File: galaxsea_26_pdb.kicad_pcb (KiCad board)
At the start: 2 copper layers, 80 x 50 mm, 27 parts, among them J1 Conn_01x10_Pin, J2 Conn_01x10_Pin, J3 Conn_01x10_Pin, U1 TPS54531DDA

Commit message: Dimensions
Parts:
- moved G*** 40.8 mm to (116.4, 63.4)
- moved D2 5.60 mm to (131.1, 71.7)
- moved D3 5.60 mm to (136.5, 71.7)
- moved R4 5.60 mm to (131.1, 76.0)
- moved R5 5.60 mm to (136.5, 76.0)
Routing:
- net /BDC Module/BDC_VOUT: track 86.6 -> 80.4 mm
- net /BDC Module/BDC_VIN_Fuse: track 29.7 -> 24.7 mm
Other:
- outline, holes or cut-outs redrawn

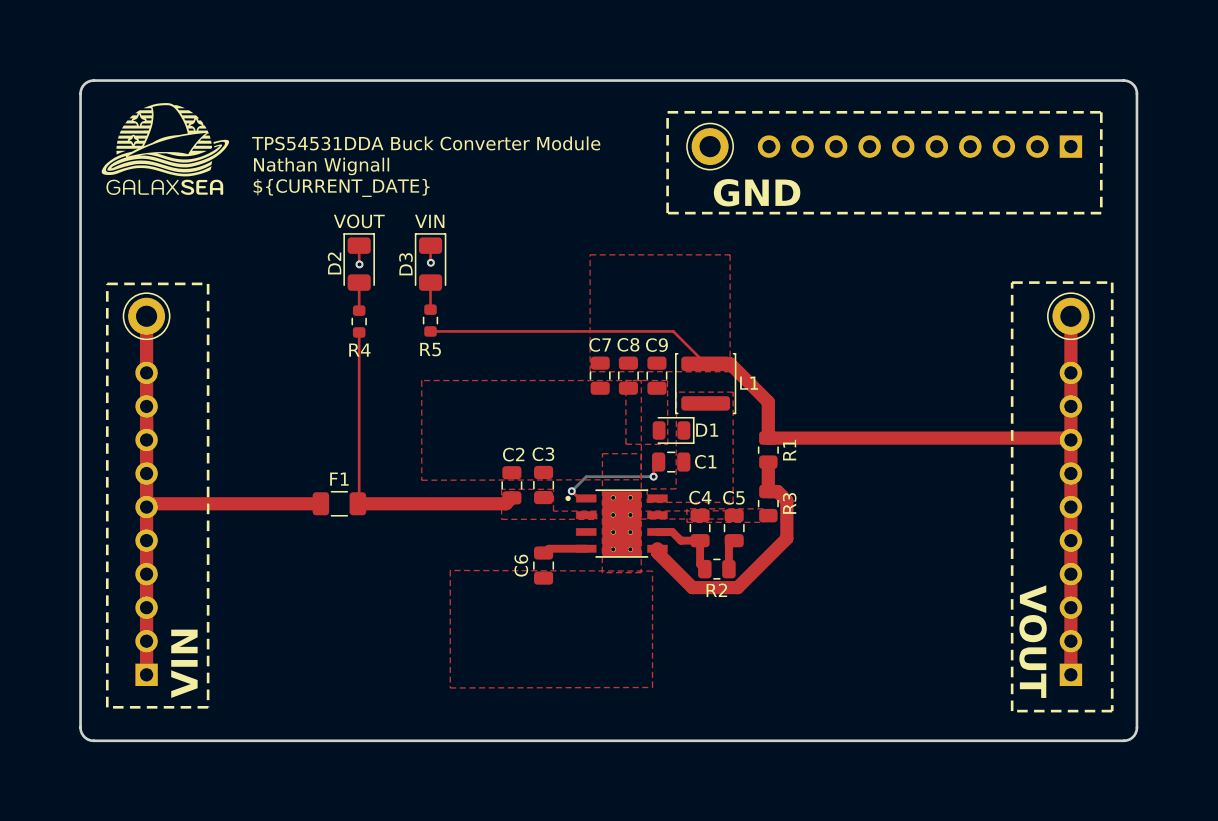
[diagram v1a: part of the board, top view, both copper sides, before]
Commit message: Make square
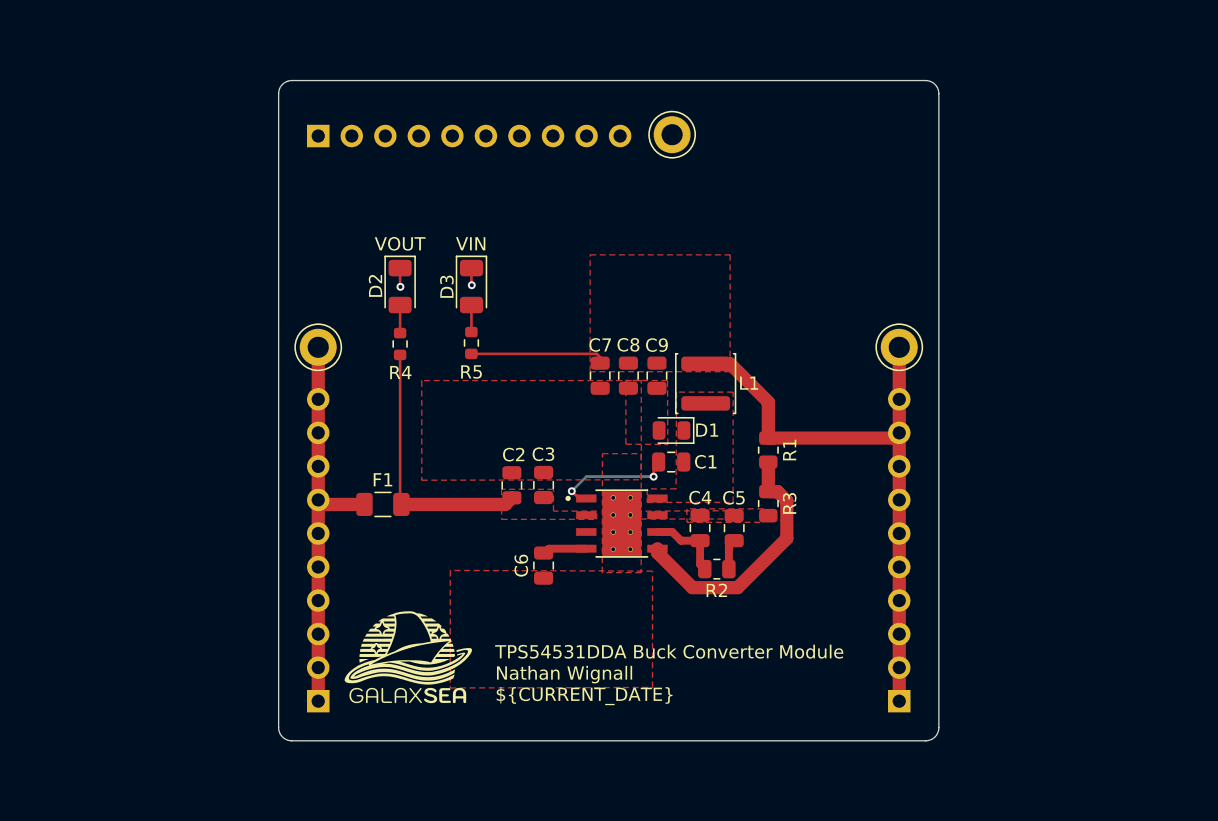
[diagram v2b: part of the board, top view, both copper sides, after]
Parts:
- moved J3 57.0 mm to (128.0, 62.0), turned to -90 degrees
- moved G*** 42.7 mm to (134.8, 101.9)
- moved TP1 13.2 mm to (128.0, 78.0)
- moved TP2 13.2 mm to (172.0, 78.0)
- moved J1 13.2 mm to (128.0, 104.8)
- moved J2 13.2 mm to (172.0, 104.8)
- moved D2 3.54 mm to (134.2, 73.4)
- moved D3 3.54 mm to (139.6, 73.4)
- moved R4 3.54 mm to (134.2, 77.8)
- moved R5 3.54 mm to (139.6, 77.7)
- moved F1 3.30 mm to (132.9, 89.9)
- moved TP3 3.01 mm to (154.8, 61.9)
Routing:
- net /BDC Module/BDC_VOUT: track 80.4 -> 55.9 mm
- net /BDC Module/BDC_VIN: track 41.8 -> 30.4 mm
- net /BDC Module/BDC_VIN_Fuse: track 24.7 -> 19.8 mm
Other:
- board size 80 x 50 mm -> 50 x 50 mm
- board text removed: "GND"

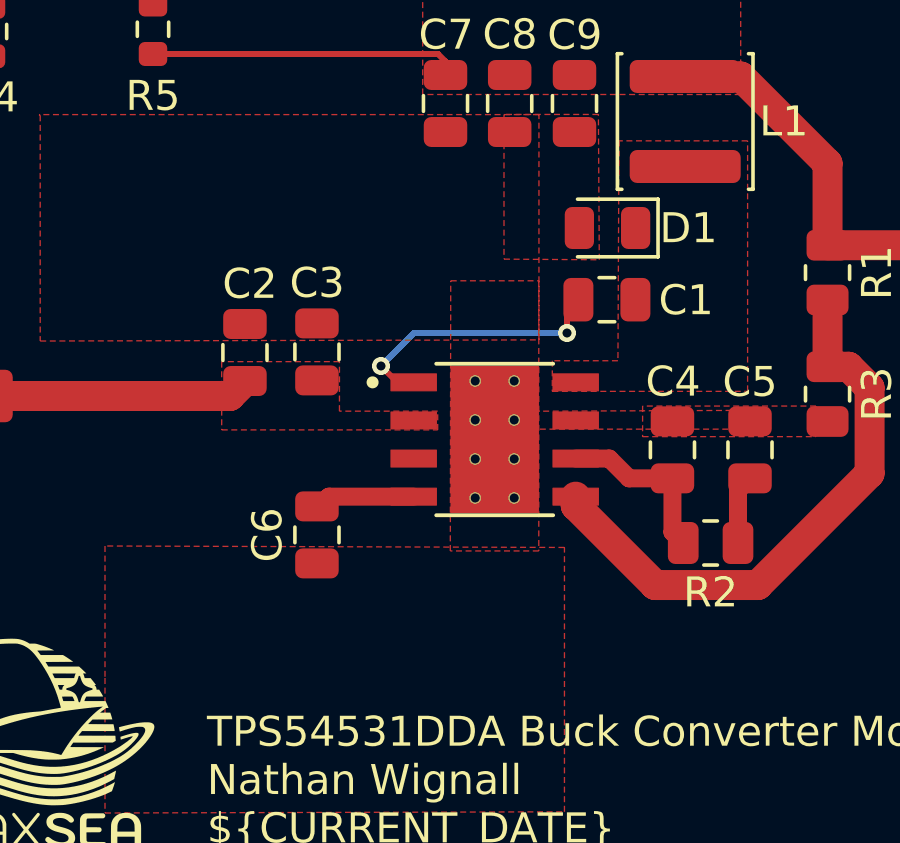
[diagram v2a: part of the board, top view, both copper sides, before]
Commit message: Ground vias
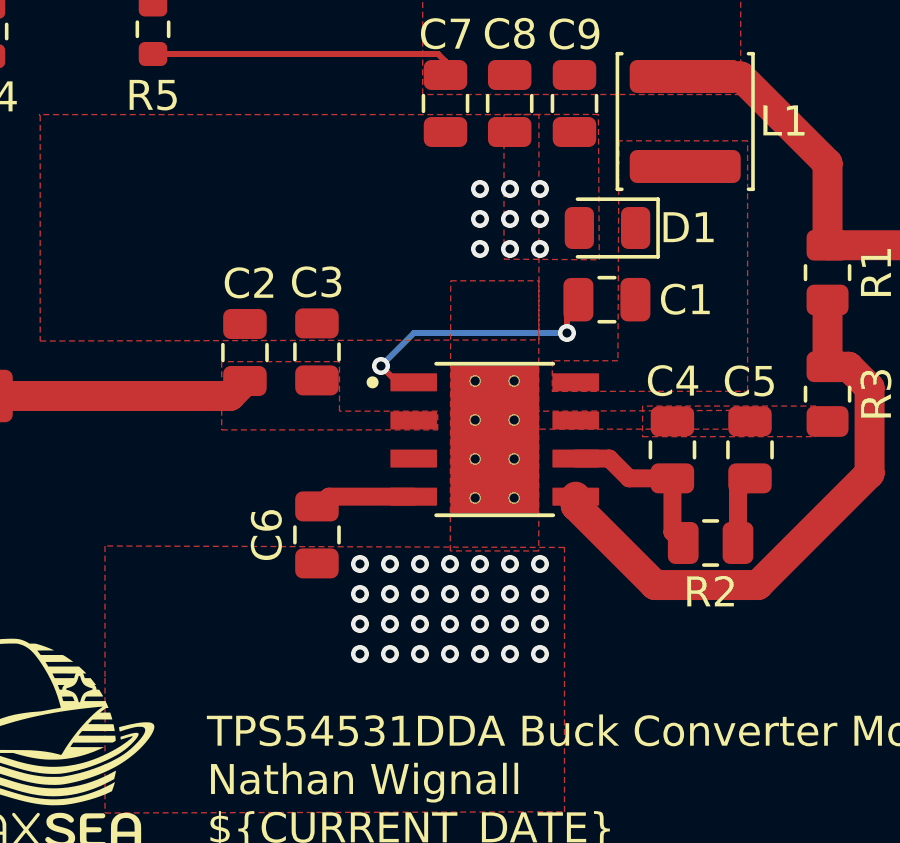
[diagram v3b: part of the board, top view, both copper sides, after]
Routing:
- net GND: vias 2 -> 39

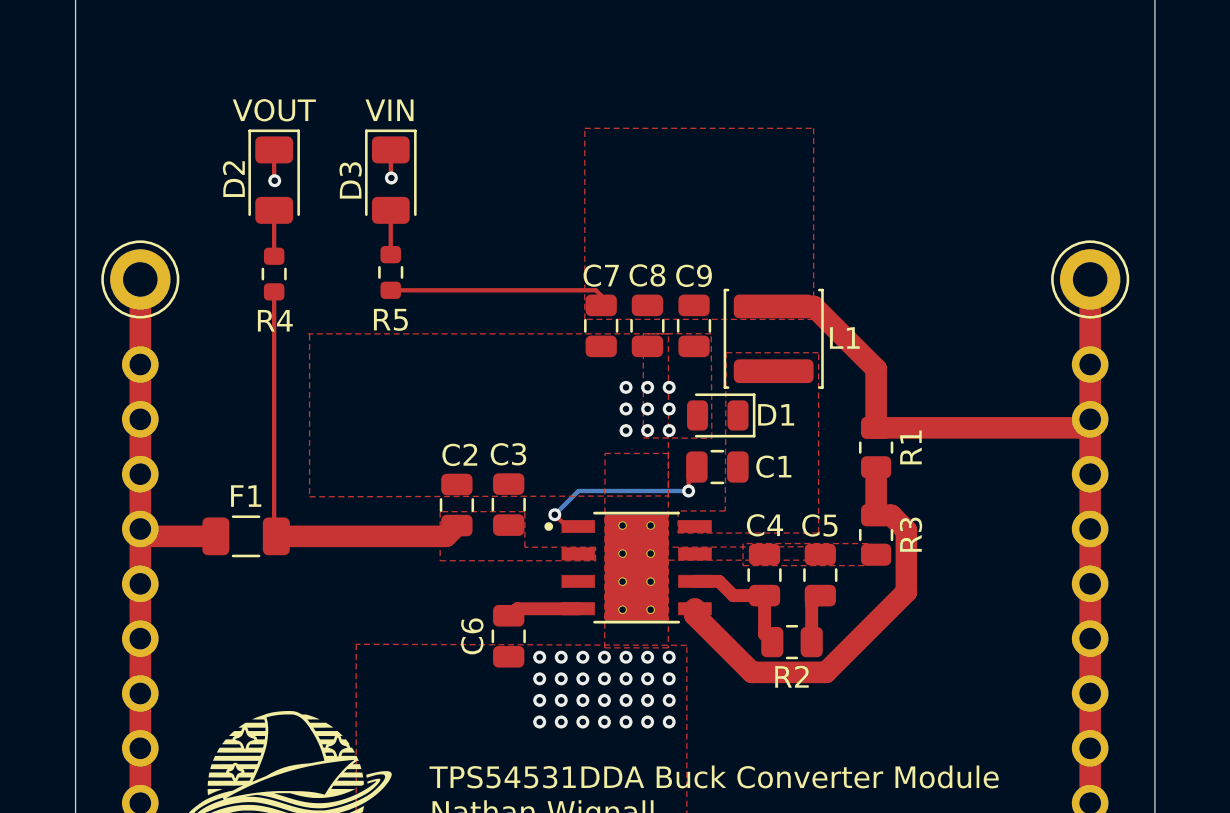
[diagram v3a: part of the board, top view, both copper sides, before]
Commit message: standardize trace width
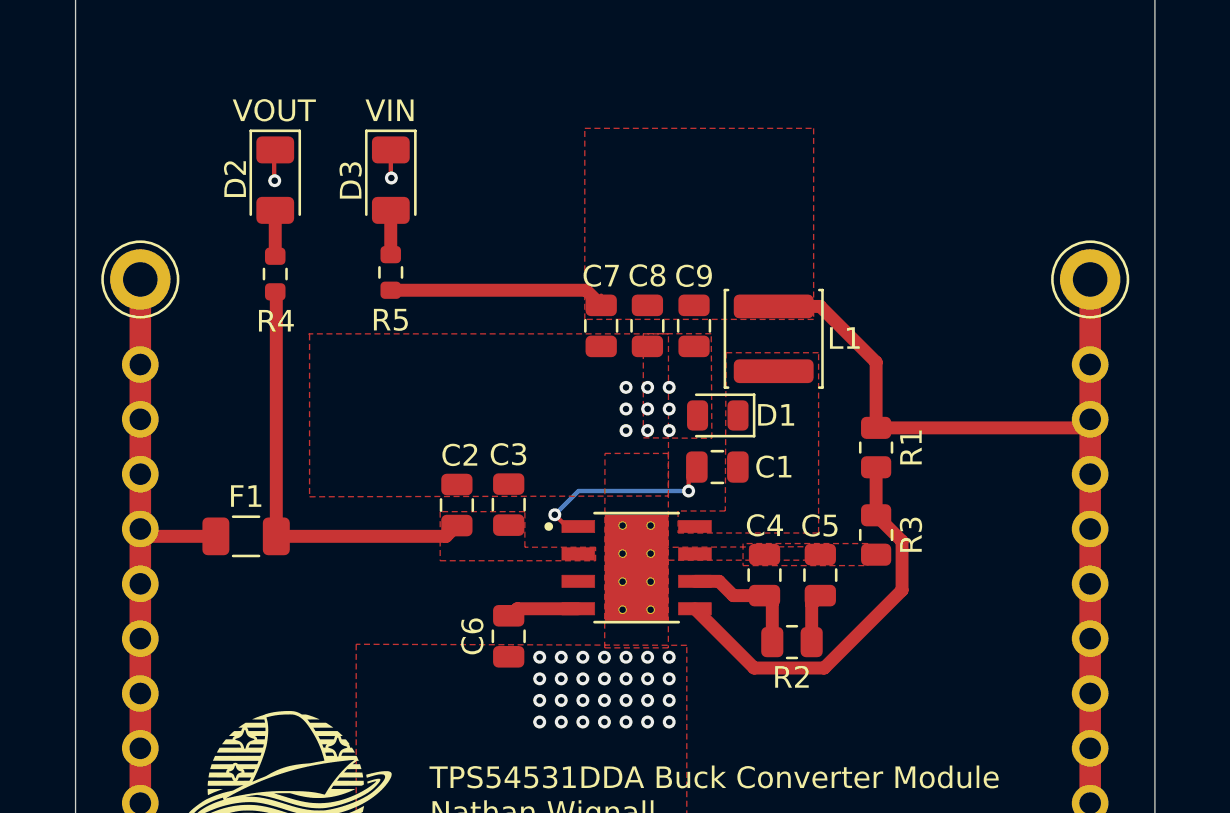
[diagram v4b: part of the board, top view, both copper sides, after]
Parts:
- moved D2 0.05 mm to (134.2, 73.4)
- moved R4 0.05 mm to (134.2, 77.8)
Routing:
- net /BDC Module/_BDC_VSENSE: track 18.9 -> 18.4 mm
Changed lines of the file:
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@@
 	(footprint "Resistor_SMD:R_0603_1608Metric"
 		(layer "F.Cu")
-		(at 134.2 77.75 90)
+		(at 134.25 77.75 90)
 		(descr "Resistor SMD 0603 (1608 Metric), square (rectangular) end terminal, IPC-7351 nominal, (Body size source: IPC-SM-782 page 72, https://www.pcb-3d.com/wordpress/wp-content/uploads/ipc-sm-782a_amendment_1_and_2.pdf), generated with kicad-footprint-generator")
 		(tags "resistor")
@@
 	(footprint "LED_SMD:LED_1206_3216Metric"
 		(layer "F.Cu")
-		(at 134.2 73.4 -90)
+		(at 134.25 73.4 -90)
 		(descr "LED SMD 1206 (3216 Metric), square (rectangular) end terminal, IPC-7351 nominal, (Body size source: http://www.tortai-tech.com/upload/download/2011102023233369053.pdf), generated with kicad-footprint-generator")
 		(tags "LED")
@@
 	)
 	(segment
-		(start 131.5 89.9)
-		(end 128.34 89.9)
-		(width 1)
+		(start 128.34 89.9)
+		(end 128 89.56)
+		(width 0.6)
 		(layer "F.Cu")
 		(net 4)
 	)
 	(segment
-		(start 128.34 89.9)
-		(end 128 89.56)
-		(width 1)
+		(start 131.5 89.9)
+		(end 128.34 89.9)
+		(width 0.6)
 		(layer "F.Cu")
 		(net 4)
@@
 	)
 	(segment
-		(start 156.915 92.645)
-		(end 155.47 92.645)
+		(start 157.275 94.8)
+		(end 157.275 93.005)
 		(width 0.6)
 		(layer "F.Cu")
@@
 	)
 	(segment
-		(start 156.915 94.44)
-		(end 157.275 94.8)
+		(start 156.915 92.645)
+		(end 155.47 92.645)
 		(width 0.6)
 		(layer "F.Cu")
@@
 	)
 	(segment
-		(start 154.81 91.985)
-		(end 153.69 91.985)
+		(start 157.275 93.005)
+		(end 156.915 92.645)
 		(width 0.6)
 		(layer "F.Cu")
@@
 	)
 	(segment
-		(start 156.915 92.645)
-		(end 156.915 94.44)
+		(start 154.81 91.985)
+		(end 153.69 91.985)
 		(width 0.6)
 		(layer "F.Cu")
@@
 	)
 	(segment
-		(start 171.605 84.875)
-		(end 172 84.48)
-		(width 1)
+		(start 139.6 78.5)
+		(end 148.65 78.5)
+		(width 0.6)
 		(layer "F.Cu")
 		(net 8)
 	)
 	(segment
-		(start 149.35 78.75)
-		(end 149.1 78.5)
-		(width 0.2)
+		(start 159.5 79.25)
+		(end 157.34 79.25)
+		(width 0.6)
 		(layer "F.Cu")
 		(net 8)
@@
 	)
 	(segment
-		(start 162.085 82.145)
-		(end 162.085 84.875)
-		(width 1)
+		(start 162.085 81.835)
+		(end 159.5 79.25)
+		(width 0.6)
 		(layer "F.Cu")
 		(net 8)
 	)
 	(segment
-		(start 157.34 79.25)
-		(end 159.19 79.25)
-		(width 1)
+		(start 171.605 84.875)
+		(end 172 84.48)
+		(width 0.6)
 		(layer "F.Cu")
 		(net 8)
 	)
 	(segment
-		(start 159.19 79.25)
-		(end 162.085 82.145)
-		(width 1)
+		(start 162.085 84.875)
+		(end 162.085 81.835)
+		(width 0.6)
 		(layer "F.Cu")
 		(net 8)
 	)
 	(segment
-		(start 139.6 78.5)
-		(end 149.1 78.5)
-		(width 0.2)
+		(start 172 78)
+		(end 172 104.8)
+		(width 1)
 		(layer "F.Cu")
 		(net 8)
 	)
 	(segment
-		(start 162.085 84.875)
-		(end 171.605 84.875)
-		(width 1)
+		(start 148.65 78.5)
+		(end 149.35 79.2)
+		(width 0.6)
 		(layer "F.Cu")
 		(net 8)
 	)
 	(segment
-		(start 172 78)
-		(end 172 104.8)
-		(width 1)
+		(start 162.085 84.875)
+		(end 171.605 84.875)
+		(width 0.6)
 		(layer "F.Cu")
 		(net 8)
 	)
 	(segment
-		(start 163.486 92.478344)
-		(end 163.486 89.626)
-		(width 1)
+		(start 153.69 93.255)
+		(end 156.436 96.001)
+		(width 0.6)
 		(layer "F.Cu")
 		(net 9)
 	)
 	(segment
-		(start 153.69 93.555)
-		(end 156.336 96.201)
-		(width 1)
+		(start 156.436 96.001)
+		(end 159.680502 96.001)
+		(width 0.6)
 		(layer "F.Cu")
 		(net 9)
 	)
 	(segment
-		(start 156.336 96.201)
-		(end 159.763344 96.201)
-		(width 1)
+		(start 162.085 88.925)
+		(end 162.085 86.7)
+		(width 0.6)
 		(layer "F.Cu")
 		(net 9)
 	)
 	(segment
-		(start 162.085 88.925)
-		(end 162.085 87.255)
-		(width 1)
+		(start 163.286 92.395502)
+		(end 163.286 90.126)
+		(width 0.6)
 		(layer "F.Cu")
 		(net 9)
 	)
 	(segment
-		(start 163.486 89.626)
-		(end 162.785 88.925)
-		(width 1)
+		(start 159.680502 96.001)
+		(end 163.286 92.395502)
+		(width 0.6)
 		(layer "F.Cu")
 		(net 9)
 	)
 	(segment
-		(start 159.763344 96.201)
-		(end 163.486 92.478344)
-		(width 1)
+		(start 163.286 90.126)
+		(end 162.085 88.925)
+		(width 0.6)
 		(layer "F.Cu")
 		(net 9)
 	)
 	(segment
-		(start 153.69 93.255)
-		(end 153.69 93.555)
-		(width 1)
+		(start 134.3 78.625)
+		(end 134.25 78.575)
+		(width 0.6)
 		(layer "F.Cu")
-		(net 9)
+		(net 11)
 	)
 	(segment
-		(start 162.785 88.925)
-		(end 162.085 88.925)
-		(width 1)
+		(start 134.3 78.675)
+		(end 134.2 78.575)
+		(width 0.6)
 		(layer "F.Cu")
-		(net 9)
+		(net 11)
 	)
 	(segment
 		(start 134.3 89.9)
 		(end 142.165 89.9)
-		(width 1)
+		(width 0.6)
 		(layer "F.Cu")
 		(net 11)
@@
 		(start 142.165 89.9)
 		(end 142.665 89.4)
-		(width 1)
+		(width 0.6)
 		(layer "F.Cu")
 		(net 11)
 	)
 	(segment
-		(start 134.2 78.575)
-		(end 134.2 89.8)
-		(width 0.2)
+		(start 134.3 89.9)
+		(end 134.3 78.625)
+		(width 0.6)
 		(layer "F.Cu")
 		(net 11)
 	)
 	(segment
-		(start 134.2 74.8)
-		(end 134.2 76.925)
-		(width 0.2)
+		(start 134.25 76.925)
+		(end 134.25 74.8)
+		(width 0.6)
 		(layer "F.Cu")
 		(net 12)
 	)
 	(segment
+		(start 139.6 74.805)
+		(end 139.605 74.8)
+		(width 0.6)
+		(layer "F.Cu")
+		(net 13)
+	)
+	(segment
 		(start 139.6 76.85)
 		(end 139.6 74.805)
-		(width 0.2)
+		(width 0.6)
 		(layer "F.Cu")
 		(net 13)

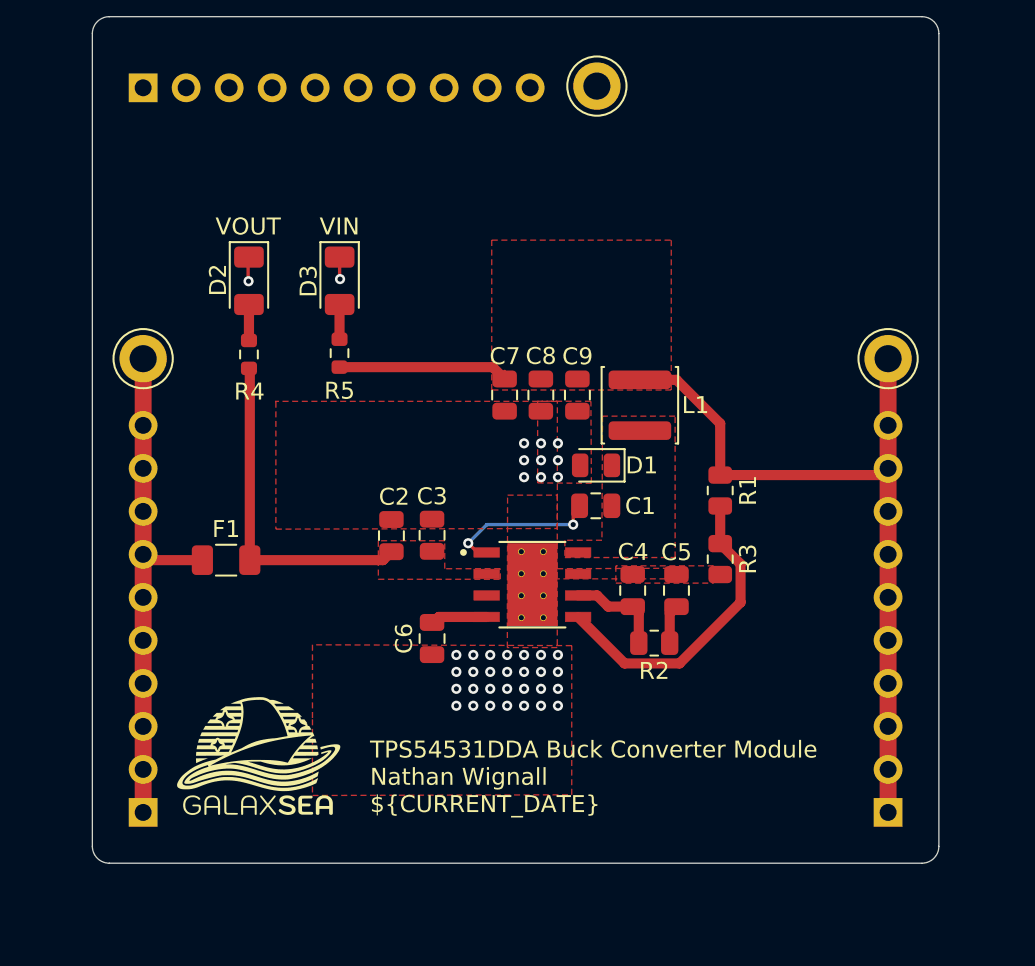
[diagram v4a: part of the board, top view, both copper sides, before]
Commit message: Add XT30 connectors
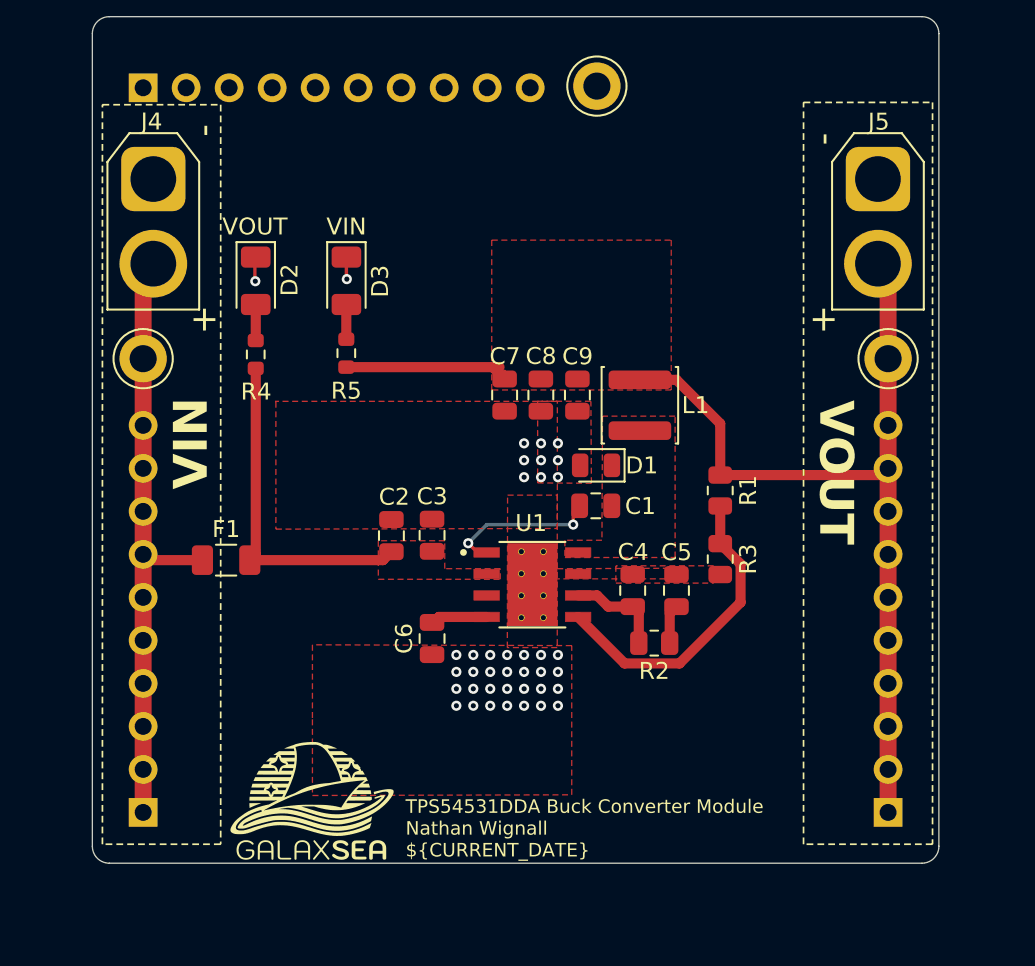
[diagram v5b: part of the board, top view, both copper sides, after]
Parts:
- added J4: Conn_01x02, Connector_AMASS:AMASS_XT30U-F_1x02_P5.0mm_Vertical, F.Cu at (128.6, 67.4)
- added J5: Conn_01x02, Connector_AMASS:AMASS_XT30U-F_1x02_P5.0mm_Vertical, F.Cu at (171.4, 67.4)
- moved G*** 4.12 mm to (138.0, 104.5)
- moved D2 0.40 mm to (134.7, 73.4)
- moved D3 0.40 mm to (140.0, 73.4)
- moved R4 0.40 mm to (134.7, 77.8)
- moved R5 0.40 mm to (140.0, 77.7)
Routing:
- net /BDC Module/BDC_VIN: track 30.4 -> 36.3 mm
- net /BDC Module/BDC_VOUT: track 56.2 -> 62.1 mm
